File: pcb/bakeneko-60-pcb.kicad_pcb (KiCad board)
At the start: 2 copper layers, 284.7 x 94.2 mm, 154 parts, among them J1 JST SH 4-pin, J2 AVR-ISP-6, SW1 Reset, U1 SRV05-4, U2 ATmega32U4-AU, Y1 16MHz

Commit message: Upgrade to Kicad 6
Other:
- outline, holes or cut-outs redrawn
- net class D removed
- net class Default removed
- net class Power removed

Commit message: Remove spacebars
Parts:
- removed the MX62 at (130.4, 85.2)
- removed MX70: 7u, MX_Only:MXOnly-7U-ReversedStabilizers-NoLED
- renumbered MX63 to MX62, MX64 to MX63, MX65 to MX64, MX66 to MX65, MX67 to MX66, MX68 to MX67, MX69 to MX68, MX72 to MX71, MX73 to MX72
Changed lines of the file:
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@@
     (at 201.88125 85.2)
     (attr through_hole)
-    (fp_text reference "MX63" (at 0 3.175) (layer "Dwgs.User")
+    (fp_text reference "MX62" (at 0 3.175) (layer "Dwgs.User")
       (effects (font (size 1 1) (thickness 0.15)))
     )
@@
     (at 225.69375 85.2)
     (attr through_hole)
-    (fp_text reference "MX64" (at 0 3.175) (layer "Dwgs.User")
+    (fp_text reference "MX63" (at 0 3.175) (layer "Dwgs.User")
       (effects (font (size 1 1) (thickness 0.15)))
     )
@@
     (at 249.50625 85.2)
     (attr through_hole)
-    (fp_text reference "MX65" (at 0 3.175) (layer "Dwgs.User")
+    (fp_text reference "MX64" (at 0 3.175) (layer "Dwgs.User")
       (effects (font (size 1 1) (thickness 0.15)))
     )
@@
     (at 273.31875 85.2)
     (attr through_hole)
-    (fp_text reference "MX66" (at 0 3.175) (layer "Dwgs.User")
+    (fp_text reference "MX65" (at 0 3.175) (layer "Dwgs.User")
       (effects (font (size 1 1) (thickness 0.15)))
     )
@@
     (at 37.575 85.2)
     (attr through_hole)
-    (fp_text reference "MX68" (at 0 3.175) (layer "Dwgs.User")
+    (fp_text reference "MX67" (at 0 3.175) (layer "Dwgs.User")
       (effects (font (size 1 1) (thickness 0.15)))
     )
@@
     (at 61.3875 85.2)
     (attr through_hole)
-    (fp_text reference "MX69" (at 0 3.175) (layer "Dwgs.User")
+    (fp_text reference "MX68" (at 0 3.175) (layer "Dwgs.User")
       (effects (font (size 1 1) (thickness 0.15)))
     )
@@
       (net 80 "COL2"))
   )
-  (footprint "MX_Only:MXOnly-7U-ReversedStabilizers-NoLED" (layer "F.Cu")
-    (at 142.35 85.2)
-    (attr through_hole)
-    (fp_text reference "MX70" (at 0 3.175) (layer "Dwgs.User")
-      (effects (font (size 1 1) (thickness 0.15)))
-    )
-    (fp_text value "7u" (at 0 -7.9375) (layer "Dwgs.User")
-      (effects (font (size 1 1) (thickness 0.15)))
-    )
-    (fp_line (start -7 7) (end -5 7) (layer "Dwgs.User") (width 0.15))
-    (fp_line (start -5 -7) (end -7 -7) (layer "Dwgs.User") (width 0.15))
-    (fp_line (start 5 -7) (end 7 -7) (layer "Dwgs.User") (width 0.15))
-    (fp_line (start -7 5) (end -7 7) (layer "Dwgs.User") (width 0.15))
-    (fp_line (start 7 -7) (end 7 -5) (layer "Dwgs.User") (width 0.15))
-    (fp_line (start 5 7) (end 7 7) (layer "Dwgs.User") (width 0.15))
-    (fp_line (start -7 -7) (end -7 -5) (layer "Dwgs.User") (width 0.15))
-    (fp_line (start 7 7) (end 7 5) (layer "Dwgs.User") (width 0.15))
-    (fp_line (start -66.675 -9.525) (end 66.675 -9.525) (layer "Dwgs.User") (width 0.15))
-    (fp_line (start 66.675 -9.525) (end 66.675 9.525) (layer "Dwgs.User") (width 0.15))
-    (fp_line (start -66.675 9.525) (end -66.675 -9.525) (layer "Dwgs.User") (width 0.15))
-    (fp_line (start -66.675 9.525) (end 66.675 9.525) (layer "Dwgs.User") (width 0.15))
-    (pad "" np_thru_hole circle locked (at -57.15 -8.255) (size 3.9878 3.9878) (drill 3.9878) (layers *.Cu *.Mask))
-    (pad "" np_thru_hole circle locked (at 0 0) (size 3.9878 3.9878) (drill 3.9878) (layers *.Cu *.Mask))
-    (pad "" np_thru_hole circle locked (at 57.15 -8.255) (size 3.9878 3.9878) (drill 3.9878) (layers *.Cu *.Mask))
-    (pad "" np_thru_hole circle locked (at -57.15 6.985) (size 3.048 3.048) (drill 3.048) (layers *.Cu *.Mask))
-    (pad "" np_thru_hole circle locked (at 5.08 0 48.0996) (size 1.75 1.75) (drill 1.75) (layers *.Cu *.Mask))
-    (pad "" np_thru_hole circle locked (at -5.08 0 48.0996) (size 1.75 1.75) (drill 1.75) (layers *.Cu *.Mask))
-    (pad "" np_thru_hole circle locked (at 57.15 6.985) (size 3.048 3.048) (drill 3.048) (layers *.Cu *.Mask))
-    (pad "1" thru_hole circle locked (at -3.81 -2.54) (size 2.25 2.25) (drill 1.47) (layers *.Cu "B.Mask")
-      (net 66 "Net-(D59-Pad2)"))
-    (pad "2" thru_hole circle locked (at 2.54 -5.08) (size 2.25 2.25) (drill 1.47) (layers *.Cu "B.Mask")
-      (net 84 "COL6"))
-  )
   (footprint "MX_Only:MXOnly-1U-NoLED" (layer "F.Cu")
     (at 247.125 85.2)
     (attr through_hole)
-    (fp_text reference "MX72" (at 0 3.175) (layer "Dwgs.User")
+    (fp_text reference "MX71" (at 0 3.175) (layer "Dwgs.User")
       (effects (font (size 1 1) (thickness 0.15)))
     )
@@
     (at 270.9375 85.2)
     (attr through_hole)
-    (fp_text reference "MX73" (at 0 3.175) (layer "Dwgs.User")
+    (fp_text reference "MX72" (at 0 3.175) (layer "Dwgs.User")
       (effects (font (size 1 1) (thickness 0.15)))
     )
@@
       (net 91 "COL13"))
   )
-  (footprint "MX_Only:MXOnly-6.25U-ReversedStabilizers-NoLED" (layer "F.Cu")
-    (at 130.44375 85.2)
-    (attr through_hole)
-    (fp_text reference "MX62" (at 0 3.175) (layer "Dwgs.User")
-      (effects (font (size 1 1) (thickness 0.15)))
-    )
-    (fp_text value "6.25u" (at 0 -7.9375) (layer "Dwgs.User")
-      (effects (font (size 1 1) (thickness 0.15)))
-    )
-    (fp_line (start 7 7) (end 7 5) (layer "Dwgs.User") (width 0.15))
-    (fp_line (start -59.53125 -9.525) (end 59.53125 -9.525) (layer "Dwgs.User") (width 0.15))
-    (fp_line (start -59.53125 9.525) (end 59.53125 9.525) (layer "Dwgs.User") (width 0.15))
-    (fp_line (start -7 -7) (end -7 -5) (layer "Dwgs.User") (width 0.15))
-    (fp_line (start -59.53125 9.525) (end -59.53125 -9.525) (layer "Dwgs.User") (width 0.15))
-    (fp_line (start -7 5) (end -7 7) (layer "Dwgs.User") (width 0.15))
-    (fp_line (start -7 7) (end -5 7) (layer "Dwgs.User") (width 0.15))
-    (fp_line (start -5 -7) (end -7 -7) (layer "Dwgs.User") (width 0.15))
-    (fp_line (start 7 -7) (end 7 -5) (layer "Dwgs.User") (width 0.15))
-    (fp_line (start 5 7) (end 7 7) (layer "Dwgs.User") (width 0.15))
-    (fp_line (start 59.53125 -9.525) (end 59.53125 9.525) (layer "Dwgs.User") (width 0.15))
-    (fp_line (start 5 -7) (end 7 -7) (layer "Dwgs.User") (width 0.15))
-    (pad "" np_thru_hole circle locked (at 5.08 0 48.0996) (size 1.75 1.75) (drill 1.75) (layers *.Cu *.Mask))
-    (pad "" np_thru_hole circle locked (at -5.08 0 48.0996) (size 1.75 1.75) (drill 1.75) (layers *.Cu *.Mask))
-    (pad "" np_thru_hole circle locked (at -49.9999 6.985) (size 3.048 3.048) (drill 3.048) (layers *.Cu *.Mask))
-    (pad "" np_thru_hole circle locked (at -49.9999 -8.255) (size 3.9878 3.9878) (drill 3.9878) (layers *.Cu *.Mask))
-    (pad "" np_thru_hole circle locked (at 0 0) (size 3.9878 3.9878) (drill 3.9878) (layers *.Cu *.Mask))
-    (pad "" np_thru_hole circle locked (at 49.9999 6.985) (size 3.048 3.048) (drill 3.048) (layers *.Cu *.Mask))
-    (pad "" np_thru_hole circle locked (at 49.9999 -8.255) (size 3.9878 3.9878) (drill 3.9878) (layers *.Cu *.Mask))
-    (pad "1" thru_hole circle locked (at -3.81 -2.54) (size 2.25 2.25) (drill 1.47) (layers *.Cu "B.Mask")
-      (net 66 "Net-(D59-Pad2)"))
-    (pad "2" thru_hole circle locked (at 2.54 -5.08) (size 2.25 2.25) (drill 1.47) (layers *.Cu "B.Mask")
-      (net 84 "COL6"))
-  )
   (footprint "MX_Only:MXOnly-1.25U-NoLED" (layer "F.Cu")
     (at 11.38125 85.2)
@@
     (at 13.7625 85.2)
     (attr through_hole)
-    (fp_text reference "MX67" (at 0 3.175) (layer "Dwgs.User")
-      (effects (font (size 1 1) (thickness 0.15)))
-    )
+    (fp_text reference "MX66" (at 0 3.175) (layer "Dwgs.User")
+      (effects (font (size 1 1) (thickness 0.15)))
+    )

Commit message: Remove unwanted bottom row 1u and 1.5u
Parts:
- removed MX66, MX68, MX71, MX72: 1.5u, MX_Only:MXOnly-1.5U-NoLED
- removed MX67, MX71: 1u, MX_Only:MXOnly-1U-NoLED

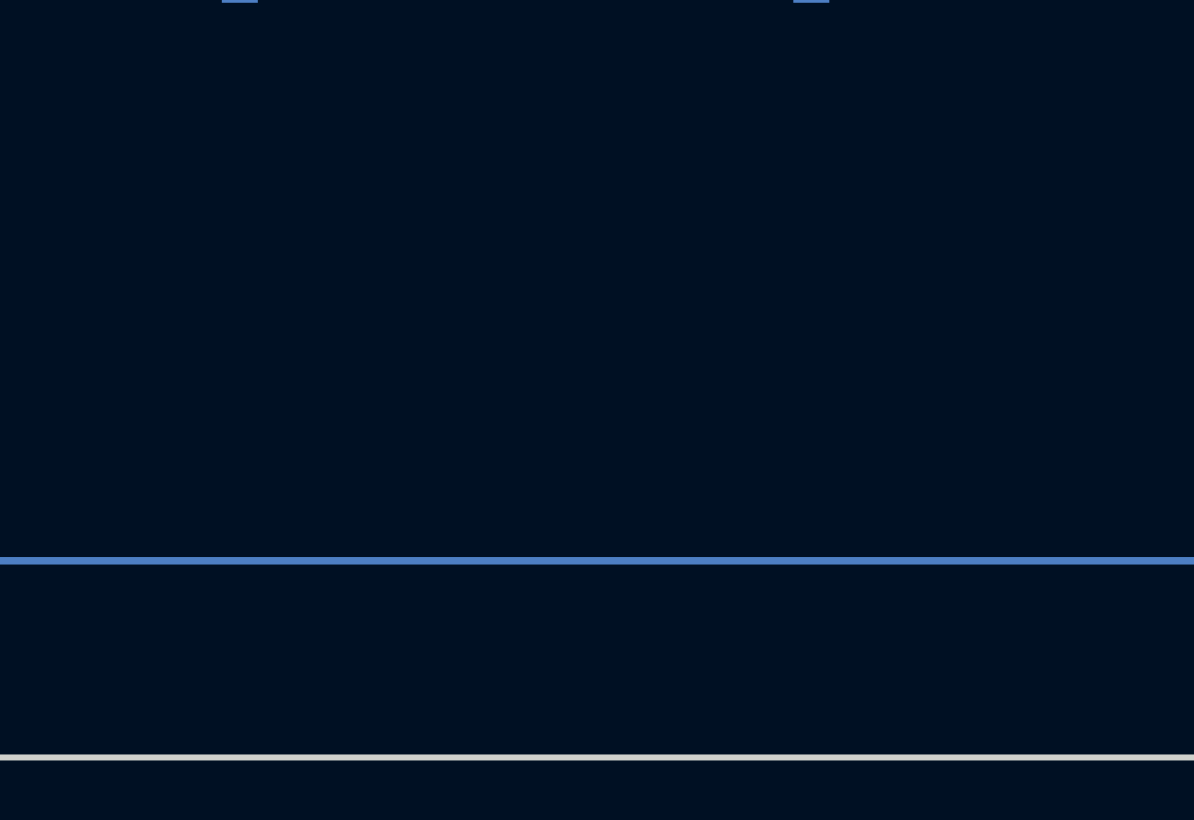
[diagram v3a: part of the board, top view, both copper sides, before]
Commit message: Place left 2.25 spacebar
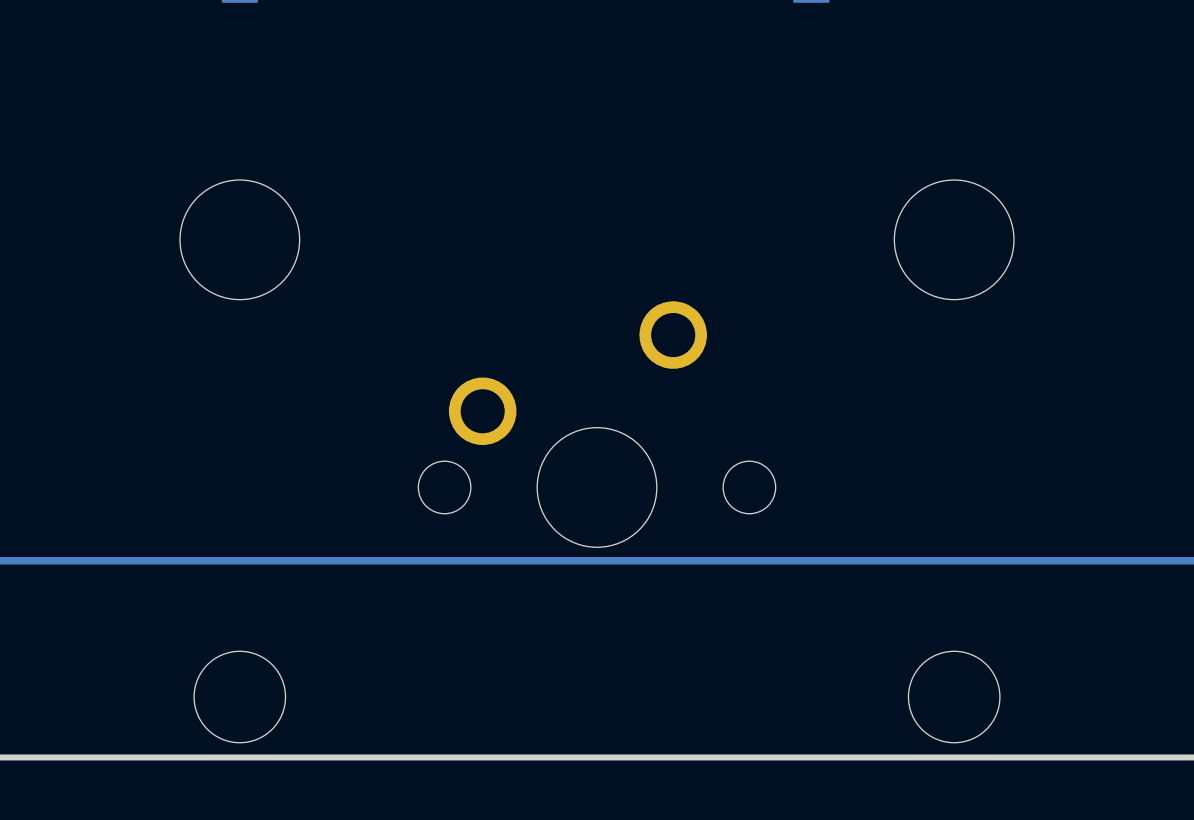
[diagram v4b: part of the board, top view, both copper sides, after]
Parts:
- added MX66: 2.25U, MX_Only:MXOnly-2.25U-ReversedStabilizers-NoLED, F.Cu at (92.3, 85.2)
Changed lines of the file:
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@@
       (net 91 "COL13"))
+  )
+  (footprint "MX_Only:MXOnly-2.25U-ReversedStabilizers-NoLED" (layer "F.Cu")
+    (at 92.34375 85.2)
+    (attr through_hole)
+    (fp_text reference "MX66" (at 0 3.175) (layer "Dwgs.User")
+      (effects (font (size 1 1) (thickness 0.15)))
+    )
+    (fp_text value "2.25U" (at 0 -7.9375) (layer "Dwgs.User")
+      (effects (font (size 1 1) (thickness 0.15)))
+    )
+    (fp_line (start 7 -7) (end 7 -5) (layer "Dwgs.User") (width 0.15))
+    (fp_line (start -7 -7) (end -7 -5) (layer "Dwgs.User") (width 0.15))
+    (fp_line (start 21.43125 -9.525) (end 21.43125 9.525) (layer "Dwgs.User") (width 0.15))
+    (fp_line (start -21.43125 9.525) (end -21.43125 -9.525) (layer "Dwgs.User") (width 0.15))
+    (fp_line (start 5 7) (end 7 7) (layer "Dwgs.User") (width 0.15))
+    (fp_line (start 7 7) (end 7 5) (layer "Dwgs.User") (width 0.15))
+    (fp_line (start -7 7) (end -5 7) (layer "Dwgs.User") (width 0.15))
+    (fp_line (start -21.43125 9.525) (end 21.43125 9.525) (layer "Dwgs.User") (width 0.15))
+    (fp_line (start -21.43125 -9.525) (end 21.43125 -9.525) (layer "Dwgs.User") (width 0.15))
+    (fp_line (start -7 5) (end -7 7) (layer "Dwgs.User") (width 0.15))
+    (fp_line (start 5 -7) (end 7 -7) (layer "Dwgs.User") (width 0.15))
+    (fp_line (start -5 -7) (end -7 -7) (layer "Dwgs.User") (width 0.15))
+    (pad "" np_thru_hole circle locked (at 0 0) (size 3.9878 3.9878) (drill 3.9878) (layers *.Cu *.Mask))
+    (pad "" np_thru_hole circle locked (at -11.90625 -8.255) (size 3.9878 3.9878) (drill 3.9878) (layers *.Cu *.Mask))
+    (pad "" np_thru_hole circle locked (at 5.08 0 48.0996) (size 1.75 1.75) (drill 1.75) (layers *.Cu *.Mask))
+    (pad "" np_thru_hole circle locked (at 11.90625 -8.255) (size 3.9878 3.9878) (drill 3.9878) (layers *.Cu *.Mask))
+    (pad "" np_thru_hole circle locked (at -11.90625 6.985) (size 3.048 3.048) (drill 3.048) (layers *.Cu *.Mask))
+    (pad "" np_thru_hole circle locked (at 11.90625 6.985) (size 3.048 3.048) (drill 3.048) (layers *.Cu *.Mask))
+    (pad "" np_thru_hole circle locked (at -5.08 0 48.0996) (size 1.75 1.75) (drill 1.75) (layers *.Cu *.Mask))
+    (pad "1" thru_hole circle locked (at -3.81 -2.54) (size 2.25 2.25) (drill 1.47) (layers *.Cu "B.Mask"))
+    (pad "2" thru_hole circle locked (at 2.54 -5.08) (size 2.25 2.25) (drill 1.47) (layers *.Cu "B.Mask"))
   )
   (footprint "MX_Only:MXOnly-1U-NoLED" (layer "F.Cu")
